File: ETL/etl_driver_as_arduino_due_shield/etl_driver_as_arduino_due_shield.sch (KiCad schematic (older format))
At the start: 10 parts, among them J1 from Arduino, J2 12V power, J3 to_ETL, Q1 BD441, U1 CA3140

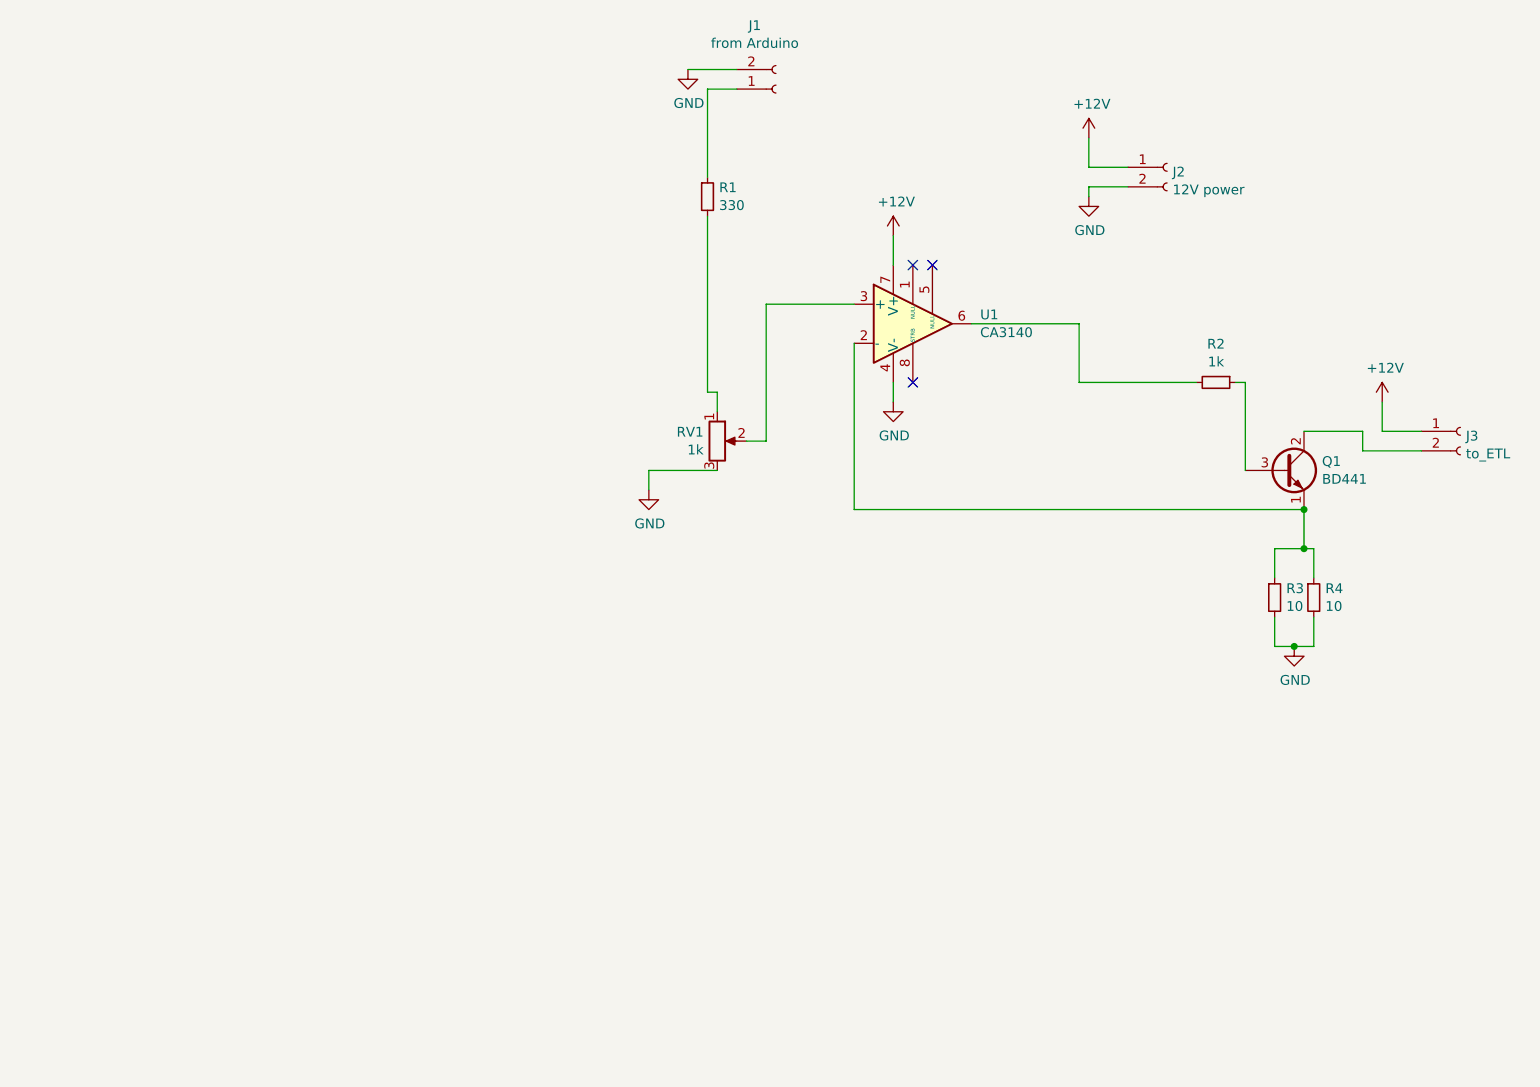
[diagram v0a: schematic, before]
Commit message: add arduino due shield for lens driver
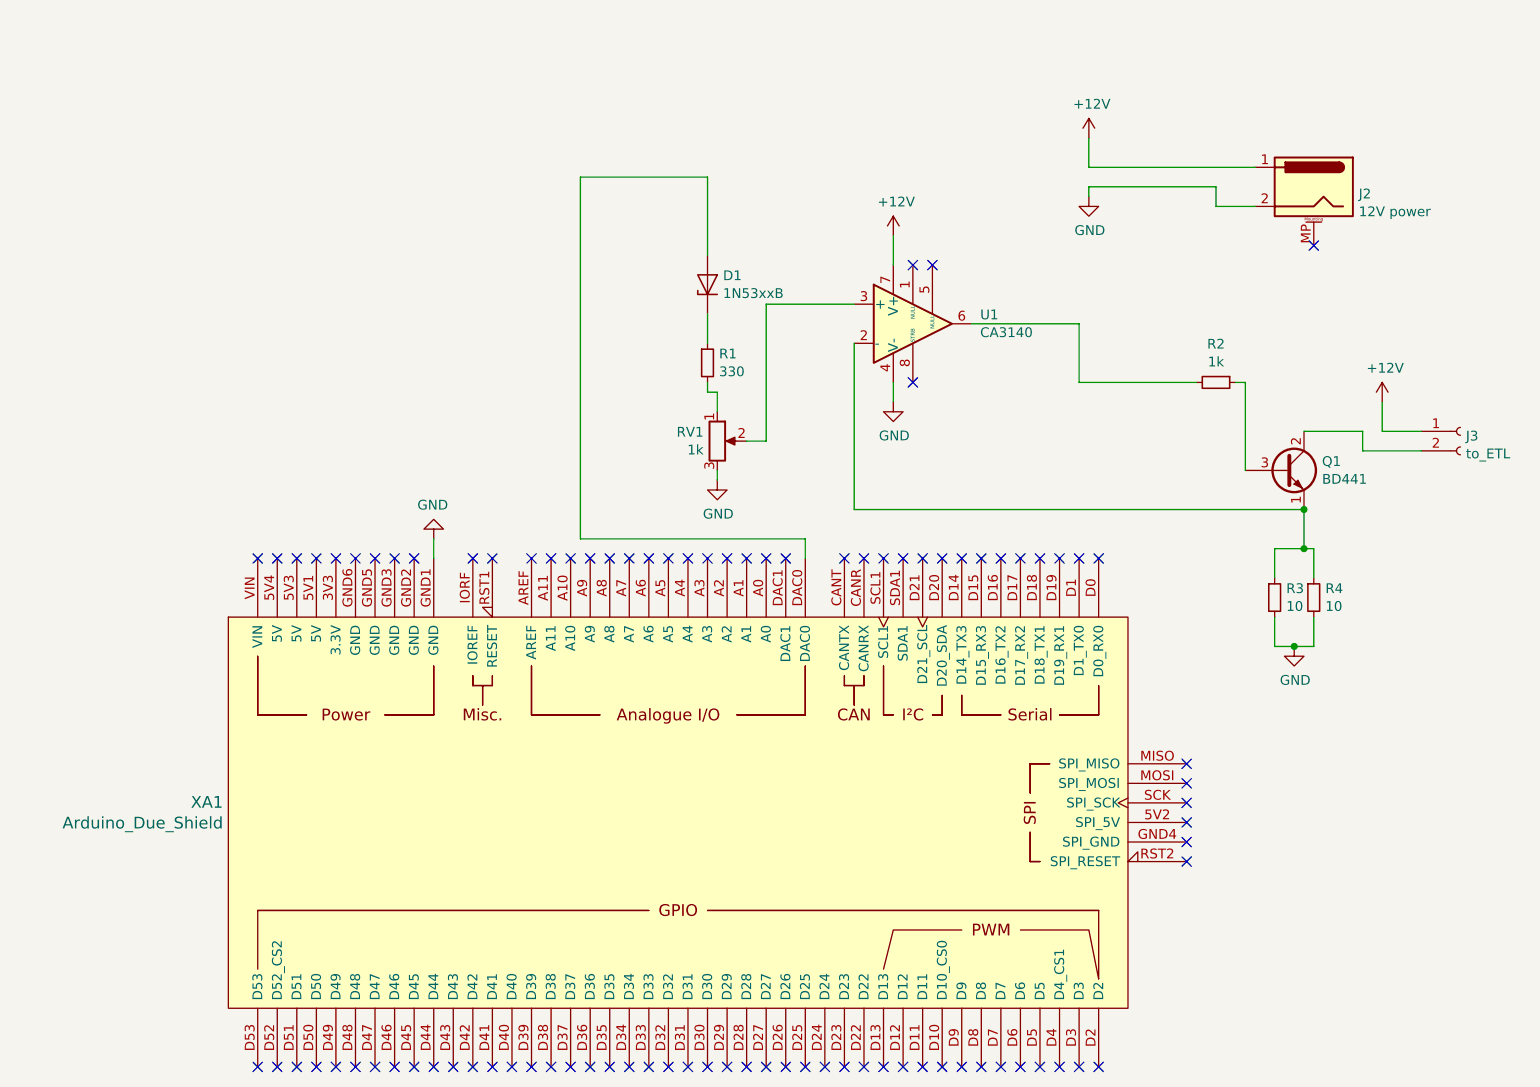
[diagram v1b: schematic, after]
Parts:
- removed J1: from Arduino, Connector_PinHeader_2.54mm:PinHeader_1x02_P2.54mm_Vertical, symbol Connector:Conn_01x02_Female
- removed J2: 12V power, Connector_PinHeader_2.54mm:PinHeader_1x02_P2.54mm_Vertical, symbol Connector:Conn_01x02_Female
- added D1: 1N53xxB, Diode_THT:D_DO-201_P15.24mm_Horizontal, symbol Diode:1N53xxB
- added J2: 12V power, Connector_BarrelJack:BarrelJack_Horizontal, symbol Connector:Barrel_Jack_MountingPin
- added XA1: Arduino_Due_Shield, Arduino:Arduino_Due_Shield, symbol Arduino:Arduino_Due_Shield
- J3: footprint Connector_PinHeader_2.54mm:PinHeader_1x02_P2.54mm_Vertical -> Connector_JST:JST_XH_B2B-XH-A_1x02_P2.50mm_Vertical
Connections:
- net +12V: now also J2.1
- net GND: now also J2.2, XA1.GND1 (GND)
- net at R1.1: now also D1.1 (K)
- new net: D1.2 (A), XA1.DAC0
- no-connect marks 3 -> 93
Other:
- moved on the sheet: R1
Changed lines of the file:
@@
 L Device:R_Small R1
 U 1 1 5E591D42
-P 4150 3100
-F 0 "R1" H 4209 3146 50  0000 L CNN
-F 1 "330" H 4209 3055 50  0000 L CNN
-F 2 "Resistor_THT:R_Axial_DIN0207_L6.3mm_D2.5mm_P10.16mm_Horizontal" H 4150 3100 50  0001 C CNN
-F 3 "~" H 4150 3100 50  0001 C CNN
-	1    4150 3100
-	1    0    0    -1
-$EndComp
-$Comp
-L Connector:Conn_01x02_Female J1
-U 1 1 5E5922EA
-P 4500 2550
-F 0 "J1" H 4392 2225 50  0000 C CNN
-F 1 "from Arduino" H 4392 2316 50  0000 C CNN
-F 2 "Connector_PinHeader_2.54mm:PinHeader_1x02_P2.54mm_Vertical" H 4500 2550 50  0001 C CNN
-F 3 "~" H 4500 2550 50  0001 C CNN
-	1    4500 2550
-	1    0    0    1
+P 4150 3950
+F 0 "R1" H 4209 3996 50  0000 L CNN
+F 1 "330" H 4209 3905 50  0000 L CNN
+F 2 "Resistor_THT:R_Axial_DIN0207_L6.3mm_D2.5mm_P10.16mm_Horizontal" H 4150 3950 50  0001 C CNN
+F 3 "~" H 4150 3950 50  0001 C CNN
+	1    4150 3950
+	1    0    0    -1
 $EndComp
 $Comp
@@
 $EndComp
 $Comp
-L Connector:Conn_01x02_Female J2
-U 1 1 5E592F50
-P 6500 2950
-F 0 "J2" H 6528 2926 50  0000 L CNN
-F 1 "12V power" H 6528 2835 50  0000 L CNN
-F 2 "Connector_PinHeader_2.54mm:PinHeader_1x02_P2.54mm_Vertical" H 6500 2950 50  0001 C CNN
-F 3 "~" H 6500 2950 50  0001 C CNN
-	1    6500 2950
-	1    0    0    -1
-$EndComp
-$Comp
 L Connector:Conn_01x02_Female J3
 U 1 1 5E59330F
@@
 F 0 "J3" H 8028 4276 50  0000 L CNN
 F 1 "to_ETL" H 8028 4185 50  0000 L CNN
-F 2 "Connector_PinHeader_2.54mm:PinHeader_1x02_P2.54mm_Vertical" H 8000 4300 50  0001 C CNN
+F 2 "Connector_JST:JST_XH_B2B-XH-A_1x02_P2.50mm_Vertical" H 8000 4300 50  0001 C CNN
 F 3 "~" H 8000 4300 50  0001 C CNN
 	1    8000 4300
@@
 Wire Wire Line
 	6100 3100 6100 3050
-Wire Wire Line
-	6100 3050 6300 3050
 $Comp
 L power:+12V #PWR03
@@
 	6100 2800 6100 2950
 Wire Wire Line
-	6100 2950 6300 2950
-$Comp
-L power:GND #PWR01
-U 1 1 5E59CE04
-P 4050 2450
-F 0 "#PWR01" H 4050 2200 50  0001 C CNN
-F 1 "GND" H 4055 2277 50  0000 C CNN
-F 2 "" H 4050 2450 50  0001 C CNN
-F 3 "" H 4050 2450 50  0001 C CNN
-	1    4050 2450
-	1    0    0    -1
-$EndComp
-Wire Wire Line
-	4050 2450 4300 2450
-Wire Wire Line
-	4150 3000 4150 2550
-Wire Wire Line
-	4150 2550 4300 2550
-Wire Wire Line
-	4150 3200 4150 4100
-Wire Wire Line
 	4150 4100 4200 4100
 Wire Wire Line
@@
 L power:GND #PWR07
 U 1 1 5E5B4DEB
-P 3850 4600
-F 0 "#PWR07" H 3850 4350 50  0001 C CNN
-F 1 "GND" H 3855 4427 50  0000 C CNN
-F 2 "" H 3850 4600 50  0001 C CNN
-F 3 "" H 3850 4600 50  0001 C CNN
-	1    3850 4600
-	1    0    0    -1
-$EndComp
-Wire Wire Line
-	4200 4500 3850 4500
-Wire Wire Line
-	3850 4500 3850 4600
+P 4200 4550
+F 0 "#PWR07" H 4200 4300 50  0001 C CNN
+F 1 "GND" H 4205 4377 50  0000 C CNN
+F 2 "" H 4200 4550 50  0001 C CNN
+F 3 "" H 4200 4550 50  0001 C CNN
+	1    4200 4550
+	1    0    0    -1
+$EndComp
 $Comp
 L power:GND #PWR0101
@@
 Wire Wire Line
 	5100 4050 5100 4150
+Wire Wire Line
+	4150 4050 4150 4100
+$Comp
+L Diode:1N53xxB D1
+U 1 1 5EA9F29E
+P 4150 3550
+F 0 "D1" V 4196 3471 50  0000 R CNN
+F 1 "1N53xxB" V 4105 3471 50  0000 R CNN
+F 2 "Diode_THT:D_DO-201_P15.24mm_Horizontal" H 4150 3375 50  0001 C CNN
+F 3 "https://diotec.com/tl_files/diotec/files/pdf/datasheets/1n5345b.pdf" H 4150 3550 50  0001 C CNN
+	1    4150 3550
+	0    -1   -1   0
+$EndComp
+Wire Wire Line
+	4150 3700 4150 3850
+$Comp
+L Arduino:Arduino_Due_Shield XA1
+U 1 1 5EA98003
+P 4000 6250
+F 0 "XA1" V 3947 3923 60  0000 R CNN
+F 1 "Arduino_Due_Shield" V 4053 3923 60  0000 R CNN
+F 2 "Arduino:Arduino_Due_Shield" H 4700 9000 60  0001 C CNN
+F 3 "https://store.arduino.cc/arduino-due" H 4700 9000 60  0001 C CNN
+	1    4000 6250
+	0    1    1    0
+$EndComp
+NoConn ~ 6150 4950
+NoConn ~ 6050 4950
+NoConn ~ 5950 4950
+NoConn ~ 5850 4950
+NoConn ~ 5750 4950
+NoConn ~ 5650 4950
+NoConn ~ 5550 4950
+NoConn ~ 5450 4950
+NoConn ~ 5350 4950
+NoConn ~ 5250 4950
+NoConn ~ 5150 4950
+NoConn ~ 5050 4950
+NoConn ~ 4950 4950
+NoConn ~ 4850 4950
+NoConn ~ 4450 4950
+NoConn ~ 4350 4950
+NoConn ~ 4250 4950
+NoConn ~ 4150 4950
+NoConn ~ 4050 4950
+NoConn ~ 3950 4950
+NoConn ~ 3850 4950
+NoConn ~ 3750 4950
+NoConn ~ 3650 4950
+NoConn ~ 3550 4950
+NoConn ~ 3450 4950
+NoConn ~ 3350 4950
+NoConn ~ 3250 4950
+NoConn ~ 3050 4950
+NoConn ~ 2950 4950
+NoConn ~ 2350 4950
+NoConn ~ 2450 4950
+NoConn ~ 2550 4950
+NoConn ~ 2650 4950
+NoConn ~ 2250 4950
+NoConn ~ 2150 4950
+NoConn ~ 2050 4950
+NoConn ~ 1950 4950
+NoConn ~ 1850 7550
+NoConn ~ 1950 7550
+NoConn ~ 2050 7550
+NoConn ~ 2150 7550
+NoConn ~ 2250 7550
+NoConn ~ 2350 7550
+NoConn ~ 2450 7550
+NoConn ~ 2550 7550
+NoConn ~ 2650 7550
+NoConn ~ 2750 7550
+NoConn ~ 2850 7550
+NoConn ~ 2950 7550
+NoConn ~ 3050 7550
+NoConn ~ 3150 7550
+NoConn ~ 3250 7550
+NoConn ~ 3350 7550
+NoConn ~ 3450 7550
+NoConn ~ 3550 7550
+NoConn ~ 3650 7550
+NoConn ~ 3750 7550
+NoConn ~ 3850 7550
+NoConn ~ 3950 7550
+NoConn ~ 4050 7550
+NoConn ~ 4150 7550
+NoConn ~ 4250 7550
+NoConn ~ 4350 7550
+NoConn ~ 4450 7550
+NoConn ~ 4550 7550
+NoConn ~ 4650 7550
+NoConn ~ 4750 7550
+NoConn ~ 4850 7550
+NoConn ~ 4950 7550
+NoConn ~ 5050 7550
+NoConn ~ 6600 6500
+NoConn ~ 6600 6400
+NoConn ~ 6600 6300
+NoConn ~ 6600 6200
+NoConn ~ 6600 6100
+NoConn ~ 6600 6000
+NoConn ~ 5150 7550
+NoConn ~ 5250 7550
+NoConn ~ 5350 7550
+NoConn ~ 5450 7550
+NoConn ~ 5550 7550
+NoConn ~ 5650 7550
+NoConn ~ 5750 7550
+NoConn ~ 5850 7550
+NoConn ~ 5950 7550
+NoConn ~ 6050 7550
+NoConn ~ 6150 7550
+Wire Wire Line
+	4150 3000 3500 3000
+Wire Wire Line
+	3500 3000 3500 4850
+Wire Wire Line
+	3500 4850 4650 4850
+Wire Wire Line
+	4650 4850 4650 4950
+Wire Wire Line
+	4150 3000 4150 3400
+NoConn ~ 4550 4950
+Wire Wire Line
+	4200 4500 4200 4550
+$Comp
+L power:GND #PWR0102
+U 1 1 5EAE79C5
+P 2750 4850
+F 0 "#PWR0102" H 2750 4600 50  0001 C CNN
+F 1 "GND" H 2755 4677 50  0000 C CNN
+F 2 "" H 2750 4850 50  0001 C CNN
+F 3 "" H 2750 4850 50  0001 C CNN
+	1    2750 4850
+	-1   0    0    1
+$EndComp
+Wire Wire Line
+	2750 4850 2750 4950
+NoConn ~ 1850 4950
+$Comp
+L Connector:Barrel_Jack_MountingPin J2
+U 1 1 5EAFD06E
+P 7250 3050
+F 0 "J2" H 7020 3014 50  0000 R CNN
+F 1 "12V power" H 7020 2923 50  0000 R CNN
+F 2 "Connector_BarrelJack:BarrelJack_Horizontal" H 7300 3010 50  0001 C CNN
+F 3 "~" H 7300 3010 50  0001 C CNN
+	1    7250 3050
+	-1   0    0    -1
+$EndComp
+Wire Wire Line
+	6100 2950 6950 2950
+Wire Wire Line
+	6950 3150 6750 3150
+Wire Wire Line
+	6750 3150 6750 3050
+Wire Wire Line
+	6100 3050 6750 3050
+NoConn ~ 7250 3350
 $EndSCHEMATC
